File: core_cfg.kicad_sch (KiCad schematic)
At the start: 17 parts, among them U1 NX1H35 PBGA625

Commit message: SDRAM, bank5
last iteration of sdram. max optimization routing and space wise. Traced 2 frams to Bank 5. Fanout of bank 5 for DF9
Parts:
- L1, L2, L3, L4: footprint Inductor_SMD:L_0805_2012Metric_Pad1.05x1.20mm_HandSolder -> Inductor_SMD:L_0402_1005Metric_Pad0.77x0.64mm_HandSolder
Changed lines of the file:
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@@
 			)
 		)
-		(property "Footprint" "Inductor_SMD:L_0805_2012Metric_Pad1.05x1.20mm_HandSolder"
+		(property "Footprint" "Inductor_SMD:L_0402_1005Metric_Pad0.77x0.64mm_HandSolder"
 			(at 44.45 54.61 0)
 			(effects
@@
 			)
 		)
-		(property "Footprint" "Inductor_SMD:L_0805_2012Metric_Pad1.05x1.20mm_HandSolder"
+		(property "Footprint" "Inductor_SMD:L_0402_1005Metric_Pad0.77x0.64mm_HandSolder"
 			(at 158.75 54.61 0)
 			(effects
@@
 			)
 		)
-		(property "Footprint" "Inductor_SMD:L_0805_2012Metric_Pad1.05x1.20mm_HandSolder"
+		(property "Footprint" "Inductor_SMD:L_0402_1005Metric_Pad0.77x0.64mm_HandSolder"
 			(at 44.45 146.05 0)
 			(effects
@@
 			)
 		)
-		(property "Footprint" "Inductor_SMD:L_0805_2012Metric_Pad1.05x1.20mm_HandSolder"
+		(property "Footprint" "Inductor_SMD:L_0402_1005Metric_Pad0.77x0.64mm_HandSolder"
 			(at 158.75 146.05 0)
 			(effects

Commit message: full components, LEDS, changed edges
all components on pcb editor. added and  routed leds and 2 PLL. changed edges o have more space
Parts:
- C12, C3, C6, C9: footprint Capacitor_SMD:C_0402_1005Metric_Pad0.74x0.62mm_HandSolder -> Capacitor_SMD:C_0603_1608Metric_Pad1.08x0.95mm_HandSolder
- L1, L2, L3, L4: footprint Inductor_SMD:L_0402_1005Metric_Pad0.77x0.64mm_HandSolder -> Inductor_SMD:L_0603_1608Metric_Pad1.05x0.95mm_HandSolder
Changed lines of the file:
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@@
 			)
 		)
-		(property "Footprint" "Capacitor_SMD:C_0402_1005Metric_Pad0.74x0.62mm_HandSolder"
+		(property "Footprint" "Capacitor_SMD:C_0603_1608Metric_Pad1.08x0.95mm_HandSolder"
 			(at 163.83 153.67 0)
 			(effects
@@
 			)
 		)
-		(property "Footprint" "Inductor_SMD:L_0402_1005Metric_Pad0.77x0.64mm_HandSolder"
+		(property "Footprint" "Inductor_SMD:L_0603_1608Metric_Pad1.05x0.95mm_HandSolder"
 			(at 44.45 54.61 0)
 			(effects
@@
 			)
 		)
-		(property "Footprint" "Inductor_SMD:L_0402_1005Metric_Pad0.77x0.64mm_HandSolder"
+		(property "Footprint" "Inductor_SMD:L_0603_1608Metric_Pad1.05x0.95mm_HandSolder"
 			(at 158.75 54.61 0)
 			(effects
@@
 			)
 		)
-		(property "Footprint" "Capacitor_SMD:C_0402_1005Metric_Pad0.74x0.62mm_HandSolder"
+		(property "Footprint" "Capacitor_SMD:C_0603_1608Metric_Pad1.08x0.95mm_HandSolder"
 			(at 39.37 153.67 0)
 			(effects
@@
 			)
 		)
-		(property "Footprint" "Inductor_SMD:L_0402_1005Metric_Pad0.77x0.64mm_HandSolder"
+		(property "Footprint" "Inductor_SMD:L_0603_1608Metric_Pad1.05x0.95mm_HandSolder"
 			(at 44.45 146.05 0)
 			(effects
@@
 			)
 		)
-		(property "Footprint" "Inductor_SMD:L_0402_1005Metric_Pad0.77x0.64mm_HandSolder"
+		(property "Footprint" "Inductor_SMD:L_0603_1608Metric_Pad1.05x0.95mm_HandSolder"
 			(at 158.75 146.05 0)
 			(effects
@@
 			)
 		)
-		(property "Footprint" "Capacitor_SMD:C_0402_1005Metric_Pad0.74x0.62mm_HandSolder"
+		(property "Footprint" "Capacitor_SMD:C_0603_1608Metric_Pad1.08x0.95mm_HandSolder"
 			(at 163.83 62.23 0)
 			(effects
@@
 			)
 		)
-		(property "Footprint" "Capacitor_SMD:C_0402_1005Metric_Pad0.74x0.62mm_HandSolder"
+		(property "Footprint" "Capacitor_SMD:C_0603_1608Metric_Pad1.08x0.95mm_HandSolder"
 			(at 39.37 62.23 0)
 			(effects

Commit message: CFG, bga sdram, banks to connectors, docoupling
Finished completely routing bga sdram, finished tracing Banks to connectors DF9. Finished tracing Picoblade, diode, reset supervisor. Finished tracing LEDS on bank 5. Finished decoupling all banks and core. Missing only the power tree and power rail level decoupling.
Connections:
- net VDDSEN renamed CORE_VDDSEN
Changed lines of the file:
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@@
 		)
 	)
-	(global_label "VDDSEN"
+	(global_label "CORE_VDDSEN"
 		(shape input)
 		(at 72.39 146.05 180)
@@
 		)
 		(property "Intersheetrefs" "${INTERSHEET_REFS}"
-			(at 64.148 146.05 0)
+			(at 59.3583 146.05 0)
 			(effects
 				(font

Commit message: power tree
power tree defined. Few changes remaining but almost finalized
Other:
- moved on the sheet: C1, C10, C11, C12, C2, C3, C4, C5, C6, C7, C8, C9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

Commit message: pre-order adjustments
DF9 connectors footprint adjusted.
Dimensions of board edges changed.
Placement of DF9 adjusted.
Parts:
- renumbered C6 to C1, C11 to C10, C3 to C11, C9 to C2, C5 to C3, C8 to C4, C4 to C5, C7 to C6, C2 to C7, C10 to C8, C1 to C9, L2 to L1, L3 to L2, L1 to L3
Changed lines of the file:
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@@
 		(dnp no)
 		(fields_autoplaced yes)
-		(property "Reference" "C11"
+		(property "Reference" "C10"
 			(at 191.77 144.7862 0)
 			(effects
@@
 			(project "PCB_Project"
 				(path "/ae14ff2f-b8e3-4dd1-9329-e73906805e39/77861c37-88e9-4408-9723-ec14cfd3d63b"
-					(reference "C11")
+					(reference "C10")
 					(unit 1)
 				)
@@
 		(dnp no)
 		(fields_autoplaced yes)
-		(property "Reference" "#PWR038"
+		(property "Reference" "#PWR011"
 			(at 173.228 40.64 0)
 			(effects
@@
 			(project "PCB_Project"
 				(path "/ae14ff2f-b8e3-4dd1-9329-e73906805e39/77861c37-88e9-4408-9723-ec14cfd3d63b"
-					(reference "#PWR038")
+					(reference "#PWR011")
 					(unit 1)
 				)
@@
 		(dnp no)
 		(fields_autoplaced yes)
-		(property "Reference" "C7"
+		(property "Reference" "C6"
 			(at 96.52 144.7862 0)
 			(effects
@@
 			(project "PCB_Project"
 				(path "/ae14ff2f-b8e3-4dd1-9329-e73906805e39/77861c37-88e9-4408-9723-ec14cfd3d63b"
-					(reference "C7")
+					(reference "C6")
 					(unit 1)
 				)
@@
 		(on_board yes)
 		(dnp no)
-		(property "Reference" "#PWR044"
+		(property "Reference" "#PWR010"
 			(at 171.45 154.94 0)
 			(effects
@@
 			(project "PCB_Project"
 				(path "/ae14ff2f-b8e3-4dd1-9329-e73906805e39/77861c37-88e9-4408-9723-ec14cfd3d63b"
-					(reference "#PWR044")
+					(reference "#PWR010")
 					(unit 1)
 				)
@@
 		(on_board yes)
 		(dnp no)
-		(property "Reference" "#PWR042"
+		(property "Reference" "#PWR05"
 			(at 105.41 154.94 0)
 			(effects
@@
 			(project "PCB_Project"
 				(path "/ae14ff2f-b8e3-4dd1-9329-e73906805e39/77861c37-88e9-4408-9723-ec14cfd3d63b"
-					(reference "#PWR042")
+					(reference "#PWR05")
 					(unit 1)
 				)
@@
 		(on_board yes)
 		(dnp no)
-		(property "Reference" "L2"
+		(property "Reference" "L1"
 			(at 81.28 41.91 90)
 			(effects
@@
 			(project "PCB_Project"
 				(path "/ae14ff2f-b8e3-4dd1-9329-e73906805e39/77861c37-88e9-4408-9723-ec14cfd3d63b"
-					(reference "L2")
+					(reference "L1")
 					(unit 1)
 				)
@@
 		(on_board yes)
 		(dnp no)
-		(property "Reference" "#FLG02"
+		(property "Reference" "#FLG03"
 			(at 200.66 45.085 0)
 			(effects
@@
 			(project "PCB_Project"
 				(path "/ae14ff2f-b8e3-4dd1-9329-e73906805e39/77861c37-88e9-4408-9723-ec14cfd3d63b"
-					(reference "#FLG02")
+					(reference "#FLG03")
 					(unit 1)
 				)
@@
 		(dnp no)
 		(fields_autoplaced yes)
-		(property "Reference" "C10"
+		(property "Reference" "C8"
 			(at 180.34 144.7862 0)
 			(effects
@@
 			(project "PCB_Project"
 				(path "/ae14ff2f-b8e3-4dd1-9329-e73906805e39/77861c37-88e9-4408-9723-ec14cfd3d63b"
-					(reference "C10")
+					(reference "C8")
 					(unit 1)
 				)
@@
 		(dnp no)
 		(fields_autoplaced yes)
-		(property "Reference" "#PWR041"
+		(property "Reference" "#PWR01"
 			(at 71.628 40.64 0)
 			(effects
@@
 			(project "PCB_Project"
 				(path "/ae14ff2f-b8e3-4dd1-9329-e73906805e39/77861c37-88e9-4408-9723-ec14cfd3d63b"
-					(reference "#PWR041")
+					(reference "#PWR01")
 					(unit 1)
 				)
@@
 		(dnp no)
 		(fields_autoplaced yes)
-		(property "Reference" "C5"
+		(property "Reference" "C3"
 			(at 85.09 53.3462 0)
 			(effects
@@
 			(project "PCB_Project"
 				(path "/ae14ff2f-b8e3-4dd1-9329-e73906805e39/77861c37-88e9-4408-9723-ec14cfd3d63b"
-					(reference "C5")
+					(reference "C3")
 					(unit 1)
 				)
@@
 		(on_board yes)
 		(dnp no)
-		(property "Reference" "#FLG03"
+		(property "Reference" "#FLG04"
 			(at 200.66 136.525 0)
 			(effects
@@
 			(project "PCB_Project"
 				(path "/ae14ff2f-b8e3-4dd1-9329-e73906805e39/77861c37-88e9-4408-9723-ec14cfd3d63b"
-					(reference "#FLG03")
+					(reference "#FLG04")
 					(unit 1)
 				)
@@
 		(dnp no)
 		(fields_autoplaced yes)
-		(property "Reference" "#PWR043"
+		(property "Reference" "#PWR02"
 			(at 71.628 132.08 0)
 			(effects
@@
 			(project "PCB_Project"
 				(path "/ae14ff2f-b8e3-4dd1-9329-e73906805e39/77861c37-88e9-4408-9723-ec14cfd3d63b"
-					(reference "#PWR043")
+					(reference "#PWR02")
 					(unit 1)
 				)
@@
 		(dnp no)
 		(fields_autoplaced yes)
-		(property "Reference" "C4"
+		(property "Reference" "C5"
 			(at 96.52 53.3462 0)
 			(effects
@@
 			(project "PCB_Project"
 				(path "/ae14ff2f-b8e3-4dd1-9329-e73906805e39/77861c37-88e9-4408-9723-ec14cfd3d63b"
-					(reference "C4")
+					(reference "C5")
 					(unit 1)
 				)
@@
 		(dnp no)
 		(fields_autoplaced yes)
-		(property "Reference" "C1"
+		(property "Reference" "C9"
 			(at 191.77 53.3462 0)
 			(effects
@@
 			(project ""
 				(path "/ae14ff2f-b8e3-4dd1-9329-e73906805e39/77861c37-88e9-4408-9723-ec14cfd3d63b"
-					(reference "C1")
+					(reference "C9")
 					(unit 1)
 				)
@@
 		(on_board yes)
 		(dnp no)
-		(property "Reference" "L1"
+		(property "Reference" "L3"
 			(at 195.58 41.91 90)
 			(effects
@@
 			(project ""
 				(path "/ae14ff2f-b8e3-4dd1-9329-e73906805e39/77861c37-88e9-4408-9723-ec14cfd3d63b"
-					(reference "L1")
+					(reference "L3")
 					(unit 1)
 				)
@@
 		(dnp no)
 		(fields_autoplaced yes)
-		(property "Reference" "#PWR045"
+		(property "Reference" "#PWR012"
 			(at 173.228 132.08 0)
 			(effects
@@
 			(project "PCB_Project"
 				(path "/ae14ff2f-b8e3-4dd1-9329-e73906805e39/77861c37-88e9-4408-9723-ec14cfd3d63b"
-					(reference "#PWR045")
+					(reference "#PWR012")
 					(unit 1)
 				)
@@
 		(dnp no)
 		(fields_autoplaced yes)
-		(property "Reference" "C9"
+		(property "Reference" "C2"
 			(at 73.66 144.7862 0)
 			(effects
@@
 			(project "PCB_Project"
 				(path "/ae14ff2f-b8e3-4dd1-9329-e73906805e39/77861c37-88e9-4408-9723-ec14cfd3d63b"
-					(reference "C9")
+					(reference "C2")
 					(unit 1)
 				)
@@
 		(on_board yes)
 		(dnp no)
-		(property "Reference" "L3"
+		(property "Reference" "L2"
 			(at 81.28 133.35 90)
 			(effects
@@
 			(project "PCB_Project"
 				(path "/ae14ff2f-b8e3-4dd1-9329-e73906805e39/77861c37-88e9-4408-9723-ec14cfd3d63b"
-					(reference "L3")
+					(reference "L2")
 					(unit 1)
 				)
@@
 		(dnp no)
 		(fields_autoplaced yes)
-		(property "Reference" "#PWR084"
+		(property "Reference" "#PWR06"
 			(at 93.726 33.528 0)
 			(effects
@@
 			(project ""
 				(path "/ae14ff2f-b8e3-4dd1-9329-e73906805e39/77861c37-88e9-4408-9723-ec14cfd3d63b"
-					(reference "#PWR084")
+					(reference "#PWR06")
 					(unit 1)
 				)
@@
 		(on_board yes)
 		(dnp no)
-		(property "Reference" "#PWR040"
+		(property "Reference" "#PWR03"
 			(at 105.41 63.5 0)
 			(effects
@@
 			(project "PCB_Project"
 				(path "/ae14ff2f-b8e3-4dd1-9329-e73906805e39/77861c37-88e9-4408-9723-ec14cfd3d63b"
-					(reference "#PWR040")
+					(reference "#PWR03")
 					(unit 1)
 				)
@@
 		(on_board yes)
 		(dnp no)
-		(property "Reference" "#PWR02"
+		(property "Reference" "#PWR04"
 			(at 89.408 64.77 0)
 			(effects
@@
 			(project "PCB_Project"
 				(path "/ae14ff2f-b8e3-4dd1-9329-e73906805e39/77861c37-88e9-4408-9723-ec14cfd3d63b"
-					(reference "#PWR02")
+					(reference "#PWR04")
 					(unit 1)
 				)
@@
 		(dnp no)
 		(fields_autoplaced yes)
-		(property "Reference" "C3"
+		(property "Reference" "C11"
 			(at 203.2 53.3462 0)
 			(effects
@@
 			(project "PCB_Project"
 				(path "/ae14ff2f-b8e3-4dd1-9329-e73906805e39/77861c37-88e9-4408-9723-ec14cfd3d63b"
-					(reference "C3")
+					(reference "C11")
 					(unit 1)
 				)
@@
 		(dnp no)
 		(fields_autoplaced yes)
-		(property "Reference" "#PWR03"
+		(property "Reference" "#PWR07"
 			(at 152.146 33.528 0)
 			(effects
@@
 			(project "PCB_Project"
 				(path "/ae14ff2f-b8e3-4dd1-9329-e73906805e39/77861c37-88e9-4408-9723-ec14cfd3d63b"
-					(reference "#PWR03")
+					(reference "#PWR07")
 					(unit 1)
 				)
@@
 		(dnp no)
 		(fields_autoplaced yes)
-		(property "Reference" "C6"
+		(property "Reference" "C1"
 			(at 73.66 53.3462 0)
 			(effects
@@
 			(project "PCB_Project"
 				(path "/ae14ff2f-b8e3-4dd1-9329-e73906805e39/77861c37-88e9-4408-9723-ec14cfd3d63b"
-					(reference "C6")
+					(reference "C1")
 					(unit 1)
 				)
@@
 		(on_board yes)
 		(dnp no)
-		(property "Reference" "#FLG04"
+		(property "Reference" "#FLG02"
 			(at 76.2 136.525 0)
 			(effects
@@
 			(project "PCB_Project"
 				(path "/ae14ff2f-b8e3-4dd1-9329-e73906805e39/77861c37-88e9-4408-9723-ec14cfd3d63b"
-					(reference "#FLG04")
+					(reference "#FLG02")
 					(unit 1)
 				)
@@
 		(dnp no)
 		(fields_autoplaced yes)
-		(property "Reference" "C8"
+		(property "Reference" "C4"
 			(at 85.09 144.7862 0)
 			(effects
@@
 			(project "PCB_Project"
 				(path "/ae14ff2f-b8e3-4dd1-9329-e73906805e39/77861c37-88e9-4408-9723-ec14cfd3d63b"
-					(reference "C8")
+					(reference "C4")
 					(unit 1)
 				)
@@
 		(dnp no)
 		(fields_autoplaced yes)
-		(property "Reference" "C2"
+		(property "Reference" "C7"
 			(at 180.34 53.3462 0)
 			(effects
@@
 			(project "PCB_Project"
 				(path "/ae14ff2f-b8e3-4dd1-9329-e73906805e39/77861c37-88e9-4408-9723-ec14cfd3d63b"
-					(reference "C2")
+					(reference "C7")
 					(unit 1)
 				)
@@
 		(on_board yes)
 		(dnp no)
-		(property "Reference" "#PWR01"
+		(property "Reference" "#PWR09"
 			(at 171.45 134.62 0)
 			(effects
@@
 			(project ""
 				(path "/ae14ff2f-b8e3-4dd1-9329-e73906805e39/77861c37-88e9-4408-9723-ec14cfd3d63b"
-					(reference "#PWR01")
+					(reference "#PWR09")
 					(unit 1)
 				)
@@
 		(on_board yes)
 		(dnp no)
-		(property "Reference" "#PWR039"
+		(property "Reference" "#PWR08"
 			(at 171.45 63.5 0)
 			(effects
@@
 			(project "PCB_Project"
 				(path "/ae14ff2f-b8e3-4dd1-9329-e73906805e39/77861c37-88e9-4408-9723-ec14cfd3d63b"
-					(reference "#PWR039")
+					(reference "#PWR08")
 					(unit 1)
 				)

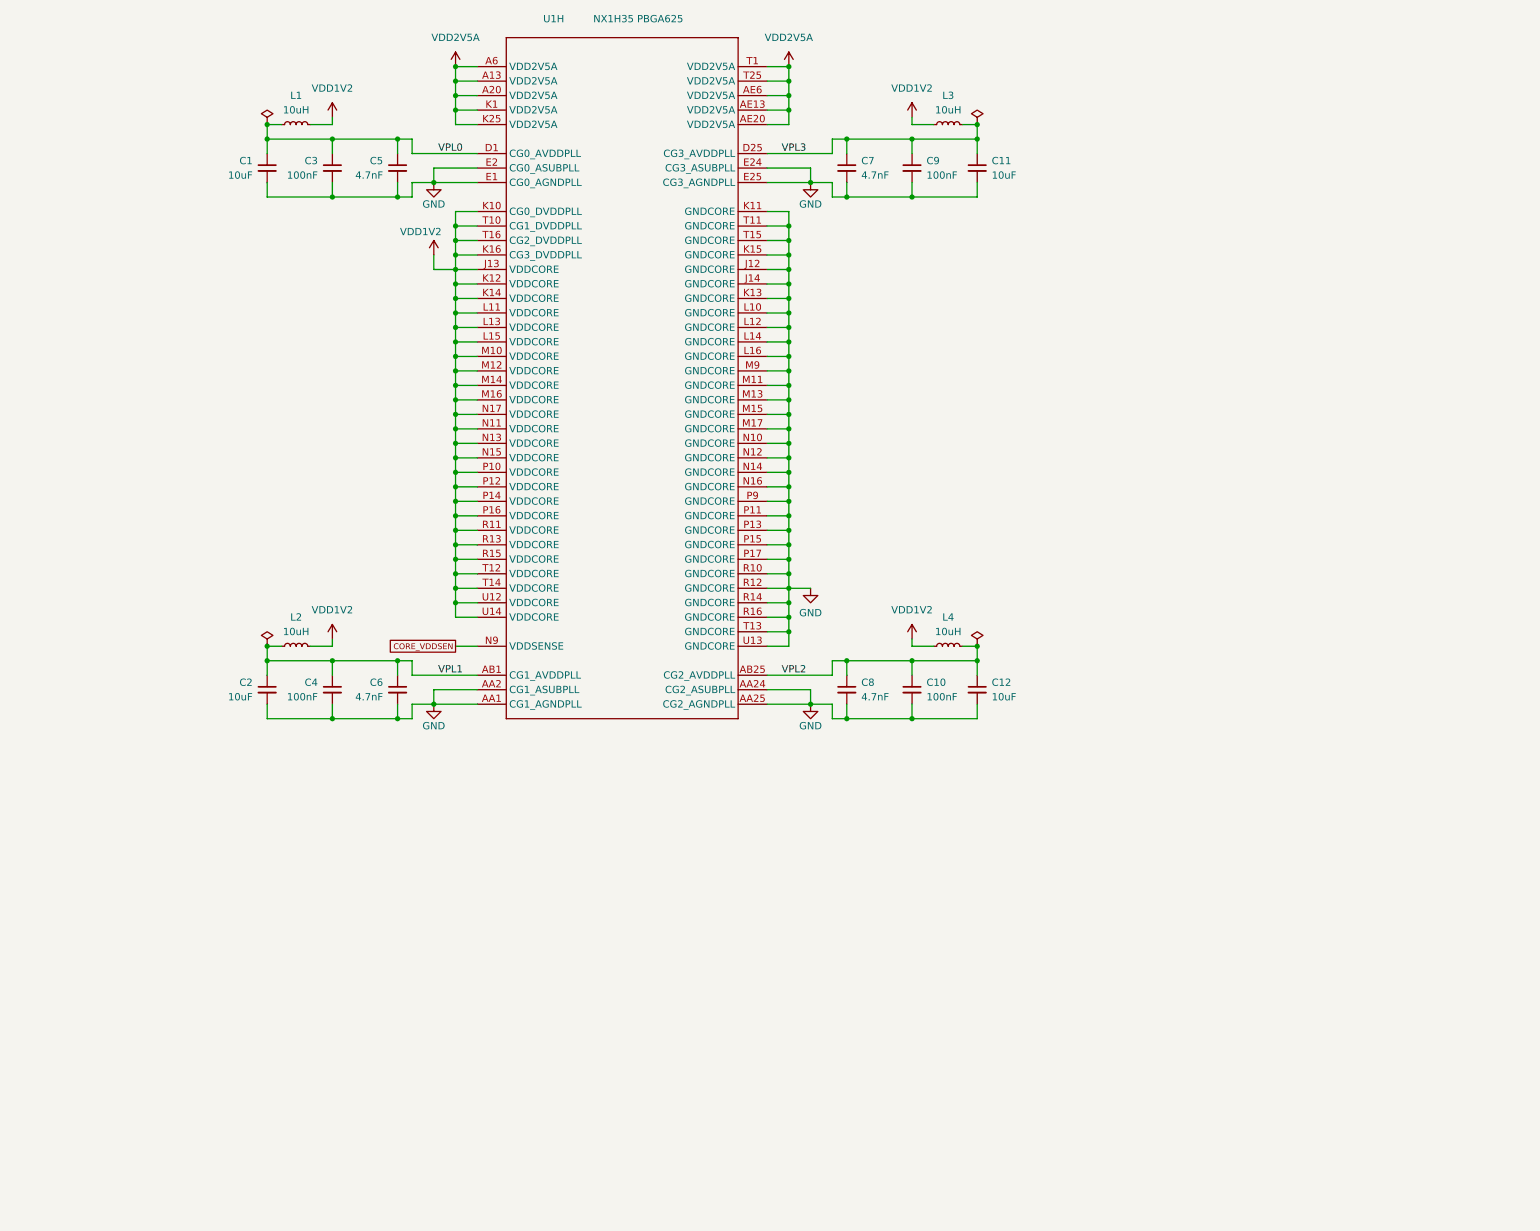
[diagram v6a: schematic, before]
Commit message: pre order adjustments. Board symmetry
adjusted little things brought up by DFM checker of JLCPCB. Board's edges fully symmetrical on y axis. 2mm shift on x axis of the DF9s maintained
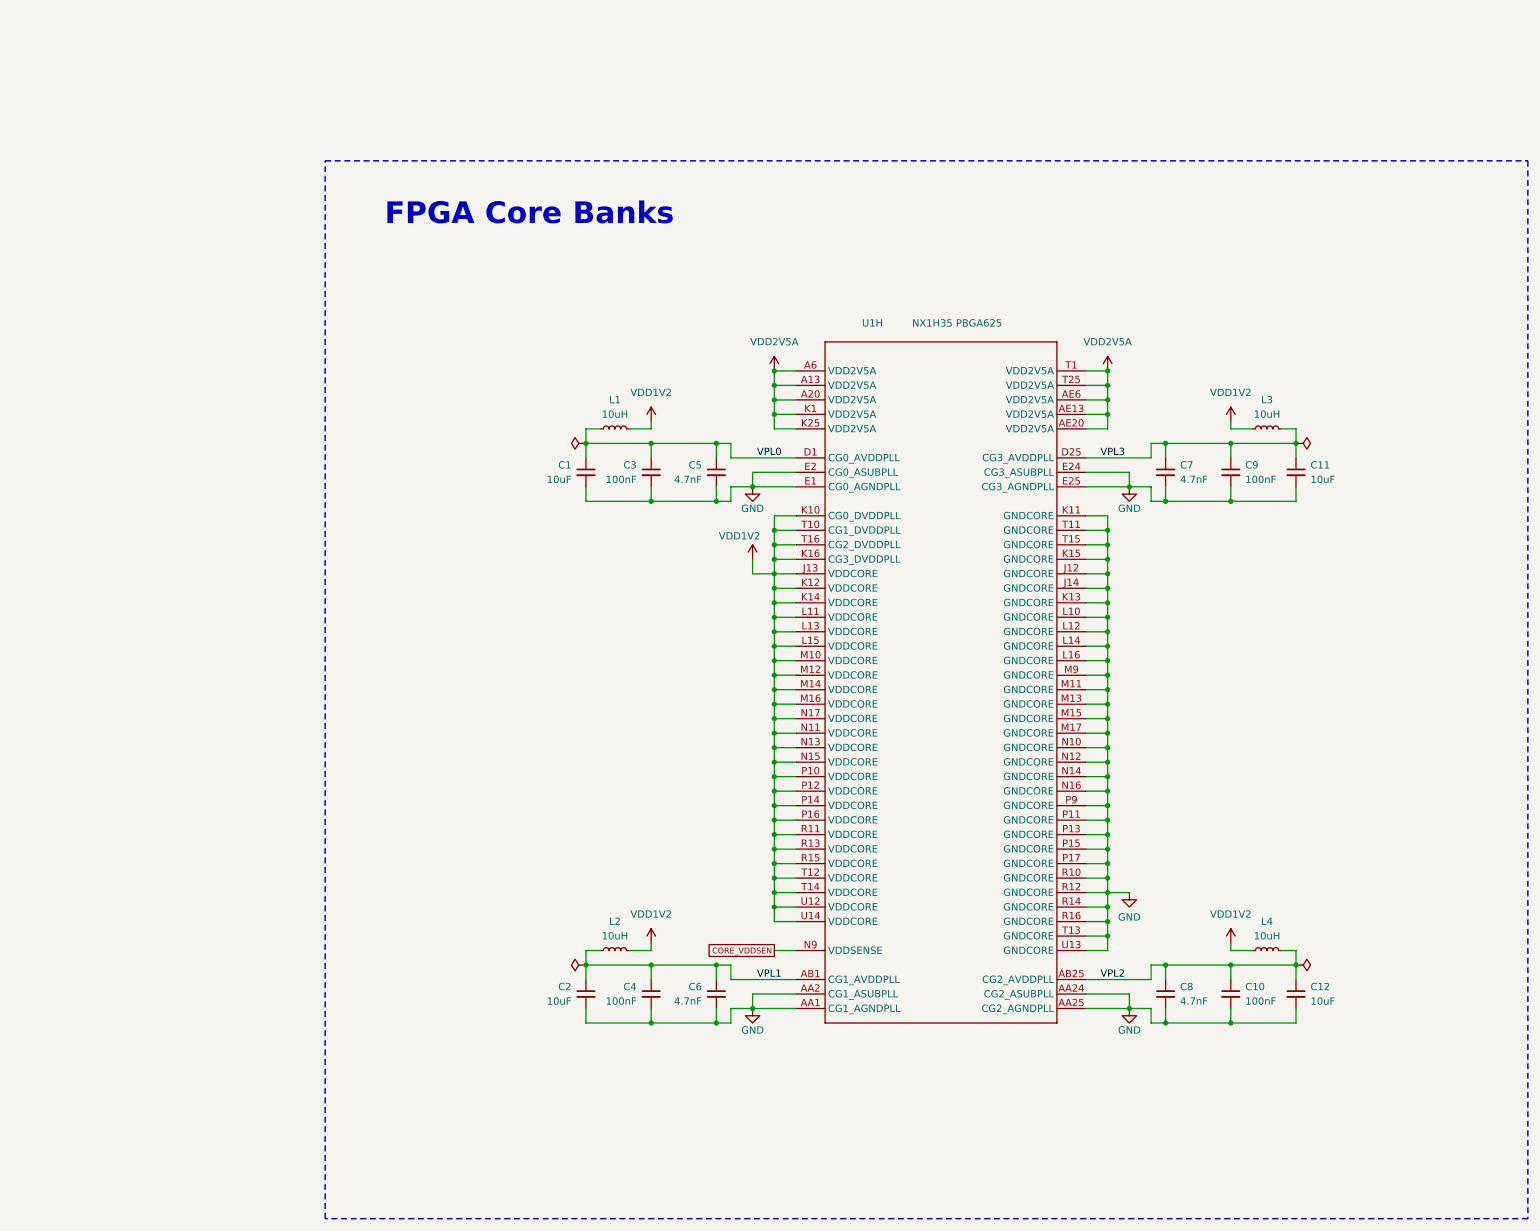
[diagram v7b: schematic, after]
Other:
- note added: "FPGA Core Banks"
- moved on the sheet: C1, C10, C11, C12, C2, C3, C4, C5, C6, C7, C8, C9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
